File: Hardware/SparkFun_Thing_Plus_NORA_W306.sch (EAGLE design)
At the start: 71 parts, among them J1 THING_PLUS_LOGICAL, J2 LiPo, J3 QWIIC_RA, J4 MICRO-SDFRICTION, J5 USB-C, J6 SWD (DNP), Q1 3.1A/30V/105mΩ, Q2 MBT3904DW1T1, U1 UBLOX_NORA_W306, U3 XC6222B331MR-G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

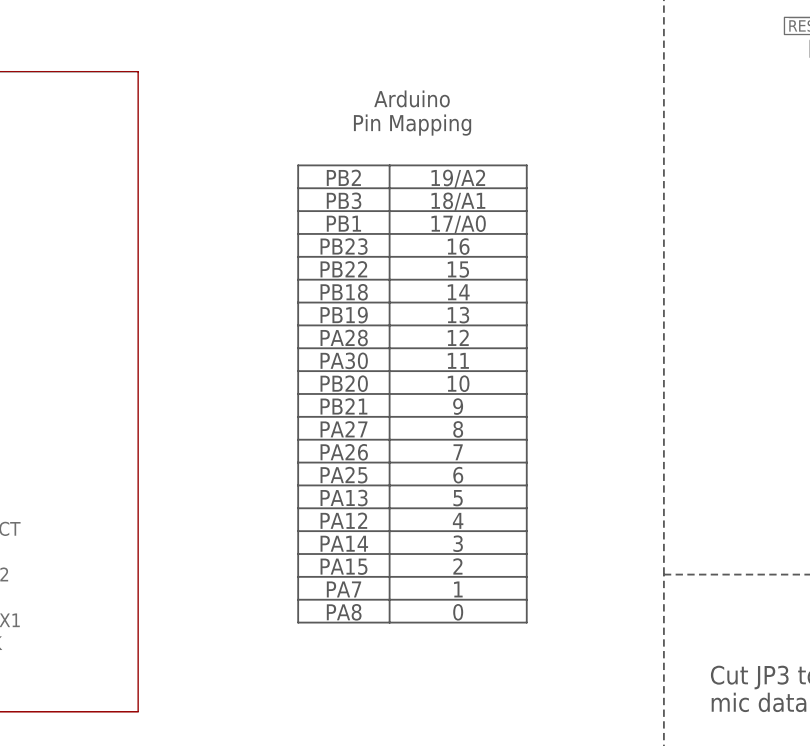
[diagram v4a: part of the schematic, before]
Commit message: Updated Arduino pin mapping table in SCH
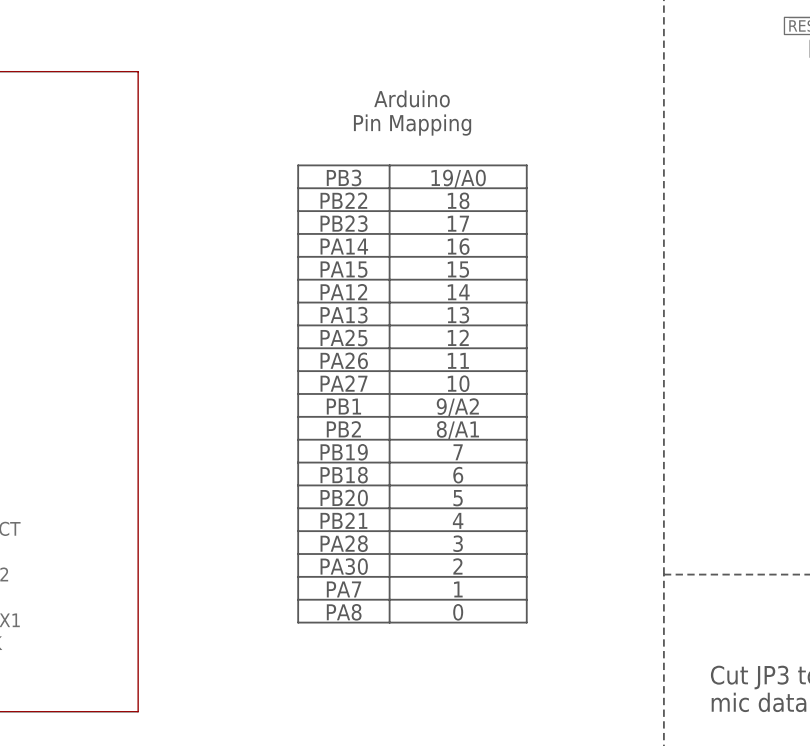
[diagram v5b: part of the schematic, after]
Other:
- note added: "17"
- note added: "18"
- note added: "19/A0"
- note added: "8/A1"
- note added: "9/A2"
- note removed: "17/A0"
- note removed: "18/A1"
- note removed: "19/A2"
- note removed: "8"
- note removed: "9"
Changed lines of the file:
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@@
 <text x="124.46" y="114.3" size="1.778" layer="97" font="vector" align="bottom-center">11</text>
 <text x="124.46" y="111.76" size="1.778" layer="97" font="vector" align="bottom-center">10</text>
-<text x="124.46" y="109.22" size="1.778" layer="97" font="vector" align="bottom-center">9</text>
-<text x="124.46" y="106.68" size="1.778" layer="97" font="vector" align="bottom-center">8</text>
+<text x="124.46" y="109.22" size="1.778" layer="97" font="vector" align="bottom-center">9/A2</text>
+<text x="124.46" y="106.68" size="1.778" layer="97" font="vector" align="bottom-center">8/A1</text>
 <text x="124.46" y="104.14" size="1.778" layer="97" font="vector" align="bottom-center">7</text>
 <text x="124.46" y="101.6" size="1.778" layer="97" font="vector" align="bottom-center">6</text>
@@
 <text x="124.46" y="88.9" size="1.778" layer="97" font="vector" align="bottom-center">1</text>
 <text x="124.46" y="86.36" size="1.778" layer="97" font="vector" align="bottom-center">0</text>
-<text x="124.46" y="134.62" size="1.778" layer="97" font="vector" align="bottom-center">19/A2</text>
-<text x="124.46" y="132.08" size="1.778" layer="97" font="vector" align="bottom-center">18/A1</text>
-<text x="124.46" y="129.54" size="1.778" layer="97" font="vector" align="bottom-center">17/A0</text>
+<text x="124.46" y="134.62" size="1.778" layer="97" font="vector" align="bottom-center">19/A0</text>
+<text x="124.46" y="132.08" size="1.778" layer="97" font="vector" align="bottom-center">18</text>
+<text x="124.46" y="129.54" size="1.778" layer="97" font="vector" align="bottom-center">17</text>
 <text x="124.46" y="127" size="1.778" layer="97" font="vector" align="bottom-center">16</text>
 <text x="124.46" y="124.46" size="1.778" layer="97" font="vector" align="bottom-center">15</text>
@@
 <text x="111.76" y="86.36" size="1.778" layer="97" font="vector" align="bottom-center">PA8</text>
 <text x="111.76" y="88.9" size="1.778" layer="97" font="vector" align="bottom-center">PA7</text>
-<text x="111.76" y="91.44" size="1.778" layer="97" font="vector" align="bottom-center">PA15</text>
-<text x="111.76" y="93.98" size="1.778" layer="97" font="vector" align="bottom-center">PA14</text>
-<text x="111.76" y="96.52" size="1.778" layer="97" font="vector" align="bottom-center">PA12</text>
-<text x="111.76" y="99.06" size="1.778" layer="97" font="vector" align="bottom-center">PA13</text>
-<text x="111.76" y="101.6" size="1.778" layer="97" font="vector" align="bottom-center">PA25</text>
-<text x="111.76" y="104.14" size="1.778" layer="97" font="vector" align="bottom-center">PA26</text>
-<text x="111.76" y="106.68" size="1.778" layer="97" font="vector" align="bottom-center">PA27</text>
-<text x="111.76" y="109.22" size="1.778" layer="97" font="vector" align="bottom-center">PB21</text>
-<text x="111.76" y="111.76" size="1.778" layer="97" font="vector" align="bottom-center">PB20</text>
-<text x="111.76" y="114.3" size="1.778" layer="97" font="vector" align="bottom-center">PA30</text>
-<text x="111.76" y="116.84" size="1.778" layer="97" font="vector" align="bottom-center">PA28</text>
-<text x="111.76" y="119.38" size="1.778" layer="97" font="vector" align="bottom-center">PB19</text>
-<text x="111.76" y="121.92" size="1.778" layer="97" font="vector" align="bottom-center">PB18</text>
-<text x="111.76" y="124.46" size="1.778" layer="97" font="vector" align="bottom-center">PB22</text>
-<text x="111.76" y="127" size="1.778" layer="97" font="vector" align="bottom-center">PB23</text>
+<text x="111.76" y="124.46" size="1.778" layer="97" font="vector" align="bottom-center">PA15</text>
+<text x="111.76" y="127" size="1.778" layer="97" font="vector" align="bottom-center">PA14</text>
+<text x="111.76" y="121.92" size="1.778" layer="97" font="vector" align="bottom-center">PA12</text>
+<text x="111.76" y="119.38" size="1.778" layer="97" font="vector" align="bottom-center">PA13</text>
+<text x="111.76" y="116.84" size="1.778" layer="97" font="vector" align="bottom-center">PA25</text>
+<text x="111.76" y="114.3" size="1.778" layer="97" font="vector" align="bottom-center">PA26</text>
+<text x="111.76" y="111.76" size="1.778" layer="97" font="vector" align="bottom-center">PA27</text>
+<text x="111.76" y="96.52" size="1.778" layer="97" font="vector" align="bottom-center">PB21</text>
+<text x="111.76" y="99.06" size="1.778" layer="97" font="vector" align="bottom-center">PB20</text>
+<text x="111.76" y="91.44" size="1.778" layer="97" font="vector" align="bottom-center">PA30</text>
+<text x="111.76" y="93.98" size="1.778" layer="97" font="vector" align="bottom-center">PA28</text>
+<text x="111.76" y="104.14" size="1.778" layer="97" font="vector" align="bottom-center">PB19</text>
+<text x="111.76" y="101.6" size="1.778" layer="97" font="vector" align="bottom-center">PB18</text>
+<text x="111.76" y="132.08" size="1.778" layer="97" font="vector" align="bottom-center">PB22</text>
+<text x="111.76" y="129.54" size="1.778" layer="97" font="vector" align="bottom-center">PB23</text>
 <text x="114.3" y="114.3" size="1.778" layer="97" font="vector" align="bottom-center"></text>
-<text x="111.76" y="129.54" size="1.778" layer="97" font="vector" align="bottom-center">PB1</text>
-<text x="111.76" y="132.08" size="1.778" layer="97" font="vector" align="bottom-center">PB3</text>
-<text x="111.76" y="134.62" size="1.778" layer="97" font="vector" align="bottom-center">PB2</text>
+<text x="111.76" y="109.22" size="1.778" layer="97" font="vector" align="bottom-center">PB1</text>
+<text x="111.76" y="134.62" size="1.778" layer="97" font="vector" align="bottom-center">PB3</text>
+<text x="111.76" y="106.68" size="1.778" layer="97" font="vector" align="bottom-center">PB2</text>
 <wire x1="116.84" y1="136.906" x2="116.84" y2="134.366" width="0.2032" layer="97"/>
 <wire x1="116.84" y1="134.366" x2="116.84" y2="131.826" width="0.2032" layer="97"/>

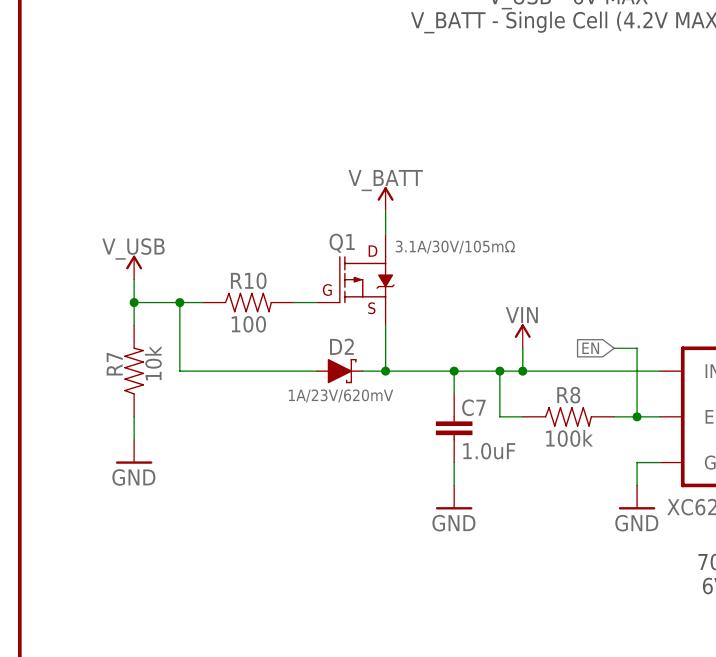
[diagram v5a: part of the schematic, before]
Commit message: Added V-MEAS jumper
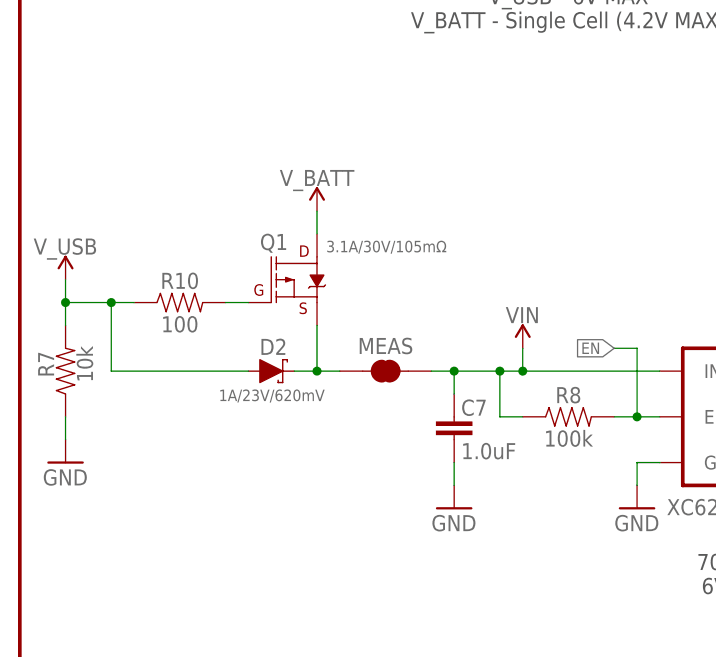
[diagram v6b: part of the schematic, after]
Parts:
- added MEAS: JUMPER-COMBO_2_NC_TRACE, SparkFun-Jumpers:JUMPER-COMBO_2_NC_TRACE
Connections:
- new net N$23: D2.C, MEAS.1, Q1.S
- net VIN: now also MEAS.2; no longer D2.C, Q1.S
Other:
- moved on the sheet: D2, Q1, R10, R7
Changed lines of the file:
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@@
 <part name="SUPPLY31" library="SparkFun-PowerSymbols" deviceset="3.3V" device=""/>
 <part name="GND33" library="SparkFun-PowerSymbols" deviceset="GND" device=""/>
+<part name="MEAS" library="SparkFun-Jumpers" deviceset="JUMPER-COMBO_2_NC_TRACE" device="" value=""/>
 </parts>
 <sheets>
@@
 <attribute name="VALUE" x="203.962" y="236.601" size="1.778" layer="96" font="vector"/>
 </instance>
-<instance part="D2" gate="G$1" x="35.56" y="226.06" smashed="yes">
-<attribute name="NAME" x="37.338" y="229.6414" size="1.778" layer="95" font="vector" rot="R180"/>
-<attribute name="VALUE" x="29.718" y="222.7326" size="1.27" layer="96" font="vector"/>
-</instance>
-<instance part="R7" gate="G$1" x="12.7" y="226.06" smashed="yes" rot="R90">
-<attribute name="NAME" x="11.43" y="226.822" size="1.778" layer="95" font="vector" rot="R90" align="bottom-center"/>
-<attribute name="VALUE" x="13.97" y="226.822" size="1.778" layer="96" font="vector" rot="R90" align="top-center"/>
-</instance>
-<instance part="GND13" gate="1" x="12.7" y="215.9" smashed="yes">
-<attribute name="VALUE" x="10.16" y="213.36" size="1.778" layer="96" font="vector"/>
+<instance part="D2" gate="G$1" x="27.94" y="226.06" smashed="yes">
+<attribute name="NAME" x="29.718" y="229.6414" size="1.778" layer="95" font="vector" rot="R180"/>
+<attribute name="VALUE" x="22.098" y="222.7326" size="1.27" layer="96" font="vector"/>
+</instance>
+<instance part="R7" gate="G$1" x="5.08" y="226.06" smashed="yes" rot="R90">
+<attribute name="NAME" x="3.81" y="226.822" size="1.778" layer="95" font="vector" rot="R90" align="bottom-center"/>
+<attribute name="VALUE" x="6.35" y="226.822" size="1.778" layer="96" font="vector" rot="R90" align="top-center"/>
+</instance>
+<instance part="GND13" gate="1" x="5.08" y="215.9" smashed="yes">
+<attribute name="VALUE" x="2.54" y="213.36" size="1.778" layer="96" font="vector"/>
 </instance>
 <instance part="J2" gate="G$1" x="223.52" y="241.3" smashed="yes" rot="R180">
@@
 <attribute name="VALUE" x="71.882" y="211.836" size="1.778" layer="96" font="vector" align="top-left"/>
 </instance>
-<instance part="Q1" gate="G$1" x="38.1" y="236.22" smashed="yes">
-<attribute name="NAME" x="34.29" y="239.522" size="1.778" layer="95" font="vector"/>
-<attribute name="VALUE" x="41.656" y="239.268" size="1.27" layer="96" font="vector"/>
+<instance part="Q1" gate="G$1" x="30.48" y="236.22" smashed="yes">
+<attribute name="NAME" x="26.67" y="239.522" size="1.778" layer="95" font="vector"/>
+<attribute name="VALUE" x="34.036" y="239.268" size="1.27" layer="96" font="vector"/>
 </instance>
 <instance part="R6" gate="G$1" x="180.34" y="223.52" smashed="yes" rot="R90">
@@
 <attribute name="VALUE" x="177.8" y="210.82" size="1.778" layer="96" font="vector"/>
 </instance>
-<instance part="R10" gate="G$1" x="25.4" y="233.68" smashed="yes">
-<attribute name="NAME" x="25.4" y="235.204" size="1.778" layer="95" font="vector" align="bottom-center"/>
-<attribute name="VALUE" x="25.4" y="232.156" size="1.778" layer="96" font="vector" align="top-center"/>
+<instance part="R10" gate="G$1" x="17.78" y="233.68" smashed="yes">
+<attribute name="NAME" x="17.78" y="235.204" size="1.778" layer="95" font="vector" align="bottom-center"/>
+<attribute name="VALUE" x="17.78" y="232.156" size="1.778" layer="96" font="vector" align="top-center"/>
 </instance>
 <instance part="R15" gate="G$1" x="269.24" y="22.86" smashed="yes" rot="R90">
@@
 <attribute name="VALUE" x="269.748" y="120.904" size="1.778" layer="96" font="vector" rot="MR180"/>
 </instance>
-<instance part="SUPPLY12" gate="G$1" x="12.7" y="236.22" smashed="yes">
-<attribute name="VALUE" x="12.7" y="239.014" size="1.778" layer="96" font="vector" align="bottom-center"/>
-</instance>
-<instance part="SUPPLY15" gate="G$1" x="40.64" y="243.84" smashed="yes">
-<attribute name="VALUE" x="40.64" y="246.634" size="1.778" layer="96" font="vector" align="bottom-center"/>
+<instance part="SUPPLY12" gate="G$1" x="5.08" y="236.22" smashed="yes">
+<attribute name="VALUE" x="5.08" y="239.014" size="1.778" layer="96" font="vector" align="bottom-center"/>
+</instance>
+<instance part="SUPPLY15" gate="G$1" x="33.02" y="243.84" smashed="yes">
+<attribute name="VALUE" x="33.02" y="246.634" size="1.778" layer="96" font="vector" align="bottom-center"/>
 </instance>
 <instance part="SUPPLY17" gate="G$1" x="55.88" y="228.6" smashed="yes">
@@
 <instance part="GND33" gate="1" x="96.52" y="43.18" smashed="yes">
 <attribute name="VALUE" x="93.98" y="40.64" size="1.778" layer="96" font="vector"/>
+</instance>
+<instance part="MEAS" gate="JP1" x="40.64" y="226.06" smashed="yes">
+<attribute name="NAME" x="40.64" y="228.854" size="1.778" layer="95" font="vector" align="center"/>
+<attribute name="VALUE" x="40.64" y="223.266" size="1.778" layer="96" font="vector" align="center"/>
 </instance>
 </instances>
@@
 <pinref part="R7" gate="G$1" pin="1"/>
 <pinref part="GND13" gate="1" pin="GND"/>
-<wire x1="12.7" y1="218.44" x2="12.7" y2="220.98" width="0.1524" layer="91"/>
+<wire x1="5.08" y1="218.44" x2="5.08" y2="220.98" width="0.1524" layer="91"/>
 </segment>
 <segment>
@@
 </segment>
 <segment>
-<wire x1="17.78" y1="233.68" x2="12.7" y2="233.68" width="0.1524" layer="91"/>
-<wire x1="17.78" y1="233.68" x2="17.78" y2="226.06" width="0.1524" layer="91"/>
-<junction x="17.78" y="233.68"/>
+<wire x1="10.16" y1="233.68" x2="5.08" y2="233.68" width="0.1524" layer="91"/>
+<wire x1="10.16" y1="233.68" x2="10.16" y2="226.06" width="0.1524" layer="91"/>
+<junction x="10.16" y="233.68"/>
 <pinref part="D2" gate="G$1" pin="A"/>
-<wire x1="17.78" y1="226.06" x2="33.02" y2="226.06" width="0.1524" layer="91"/>
+<wire x1="10.16" y1="226.06" x2="25.4" y2="226.06" width="0.1524" layer="91"/>
 <pinref part="R7" gate="G$1" pin="2"/>
-<wire x1="12.7" y1="231.14" x2="12.7" y2="233.68" width="0.1524" layer="91"/>
-<junction x="12.7" y="233.68"/>
-<wire x1="20.32" y1="233.68" x2="17.78" y2="233.68" width="0.1524" layer="91"/>
+<wire x1="5.08" y1="231.14" x2="5.08" y2="233.68" width="0.1524" layer="91"/>
+<junction x="5.08" y="233.68"/>
+<wire x1="12.7" y1="233.68" x2="10.16" y2="233.68" width="0.1524" layer="91"/>
 <pinref part="R10" gate="G$1" pin="1"/>
 <pinref part="SUPPLY12" gate="G$1" pin="V_USB"/>
-<wire x1="12.7" y1="233.68" x2="12.7" y2="236.22" width="0.1524" layer="91"/>
+<wire x1="5.08" y1="233.68" x2="5.08" y2="236.22" width="0.1524" layer="91"/>
 </segment>
 <segment>
@@
 <wire x1="71.12" y1="226.06" x2="55.88" y2="226.06" width="0.1524" layer="91"/>
 <wire x1="55.88" y1="226.06" x2="53.34" y2="226.06" width="0.1524" layer="91"/>
-<wire x1="40.64" y1="231.14" x2="40.64" y2="226.06" width="0.1524" layer="91"/>
-<pinref part="D2" gate="G$1" pin="C"/>
-<wire x1="40.64" y1="226.06" x2="48.26" y2="226.06" width="0.1524" layer="91"/>
 <wire x1="48.26" y1="226.06" x2="53.34" y2="226.06" width="0.1524" layer="91"/>
-<wire x1="38.1" y1="226.06" x2="40.64" y2="226.06" width="0.1524" layer="91"/>
-<junction x="40.64" y="226.06"/>
 <pinref part="U3" gate="G$1" pin="IN"/>
-<pinref part="Q1" gate="G$1" pin="S"/>
 <pinref part="C7" gate="G$1" pin="1"/>
 <wire x1="48.26" y1="223.52" x2="48.26" y2="226.06" width="0.1524" layer="91"/>
@@
 <wire x1="55.88" y1="226.06" x2="55.88" y2="228.6" width="0.1524" layer="91"/>
 <junction x="55.88" y="226.06"/>
+<wire x1="45.72" y1="226.06" x2="48.26" y2="226.06" width="0.1524" layer="91"/>
+<pinref part="MEAS" gate="JP1" pin="2"/>
 </segment>
 </net>
@@
 <pinref part="Q1" gate="G$1" pin="D"/>
 <pinref part="SUPPLY15" gate="G$1" pin="V_BATT"/>
-<wire x1="40.64" y1="241.3" x2="40.64" y2="243.84" width="0.1524" layer="91"/>
+<wire x1="33.02" y1="241.3" x2="33.02" y2="243.84" width="0.1524" layer="91"/>
 </segment>
 <segment>
@@
 <segment>
 <pinref part="Q1" gate="G$1" pin="G"/>
-<wire x1="33.02" y1="233.68" x2="30.48" y2="233.68" width="0.1524" layer="91"/>
+<wire x1="25.4" y1="233.68" x2="22.86" y2="233.68" width="0.1524" layer="91"/>
 <pinref part="R10" gate="G$1" pin="2"/>
 </segment>
@@
 </segment>
 </net>
+<net name="N$23" class="0">
+<segment>
+<pinref part="Q1" gate="G$1" pin="S"/>
+<wire x1="33.02" y1="231.14" x2="33.02" y2="226.06" width="0.1524" layer="91"/>
+<pinref part="D2" gate="G$1" pin="C"/>
+<wire x1="30.48" y1="226.06" x2="33.02" y2="226.06" width="0.1524" layer="91"/>
+<junction x="33.02" y="226.06"/>
+<wire x1="33.02" y1="226.06" x2="35.56" y2="226.06" width="0.1524" layer="91"/>
+<pinref part="MEAS" gate="JP1" pin="1"/>
+</segment>
+</net>

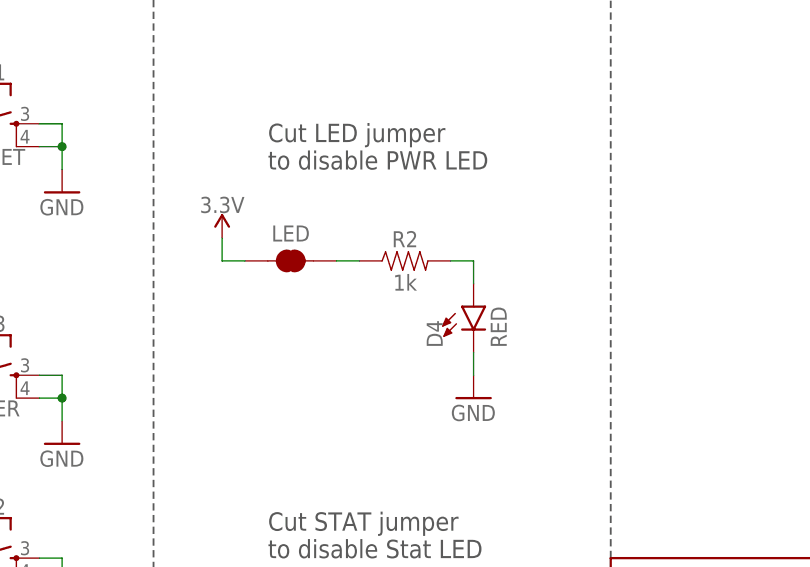
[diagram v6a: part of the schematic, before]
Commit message: Updated to new 0603 RED LED
-also updated the limiting resistor to correct value (4.7K) for DIO-17976
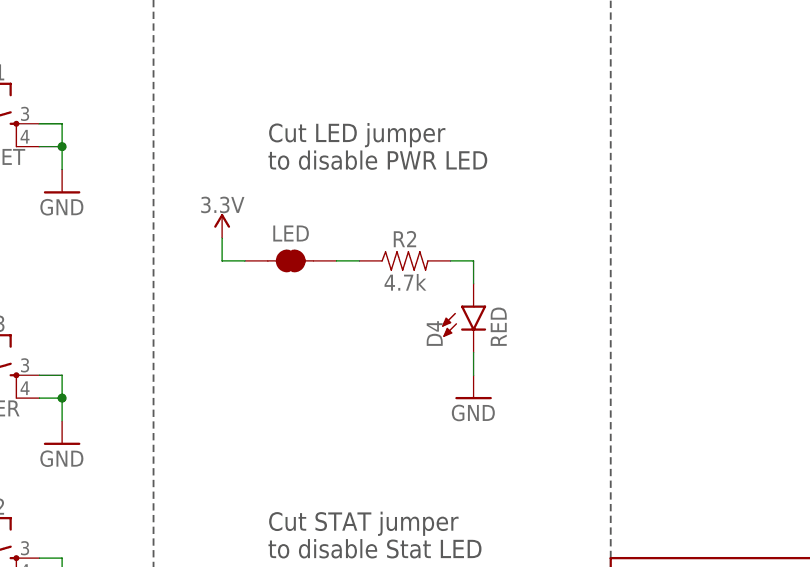
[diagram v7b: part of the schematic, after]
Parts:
- D4: device SparkFun-LED:LED-RED0603 -> SparkFun-LED:LED-RED_0603-KB
- R2: value 1k -> 4.7k; device SparkFun-Resistors:1KOHM-0402T-1/16W-1% -> SparkFun-Resistors:4.7KOHM-0402T-1/16W-1%
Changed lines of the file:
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@@
 <part name="USBSHLD" library="SparkFun-Jumpers" deviceset="JUMPER-SMT_2_NC_TRACE" device="_SILK" package3d_urn="urn:adsk.eagle:package:39281/1" value=""/>
 <part name="GND8" library="SparkFun-PowerSymbols" deviceset="GND" device=""/>
-<part name="R2" library="SparkFun-Resistors" deviceset="1KOHM" device="-0402T-1/16W-1%" value="1k"/>
+<part name="R2" library="SparkFun-Resistors" deviceset="4.7KOHM" device="-0402T-1/16W-1%" value="4.7k"/>
 <part name="LED" library="SparkFun-Jumpers" deviceset="JUMPER-SMT_2_NC_TRACE" device="_SILK" package3d_urn="urn:adsk.eagle:package:39281/1" value=""/>
 <part name="GND19" library="SparkFun-PowerSymbols" deviceset="GND" device=""/>
-<part name="D4" library="SparkFun-LED" deviceset="LED-RED" device="0603" value="RED"/>
+<part name="D4" library="SparkFun-LED" deviceset="LED-RED" device="_0603-KB" value="RED"/>
 <part name="SUPPLY8" library="SparkFun-PowerSymbols" deviceset="3.3V" device=""/>
 <part name="SUPPLY18" library="SparkFun-PowerSymbols" deviceset="V_USB" device=""/>
